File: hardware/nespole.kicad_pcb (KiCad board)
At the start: 2 copper layers, 87.9 x 54.9 mm, 45 parts, among them IC1 ATMEGA328PB-A, J1 Screw_Terminal_1x02, J2 Screw_Terminal_1x02, J3 Screw_Terminal_1x05, J4 Screw_Terminal_1x02, P1 USB_OTG, Q1 MJE13009G, Q2 MOSFET_P_CH, SW1 Rotary_Encoder_Switch, U1 MAX6675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

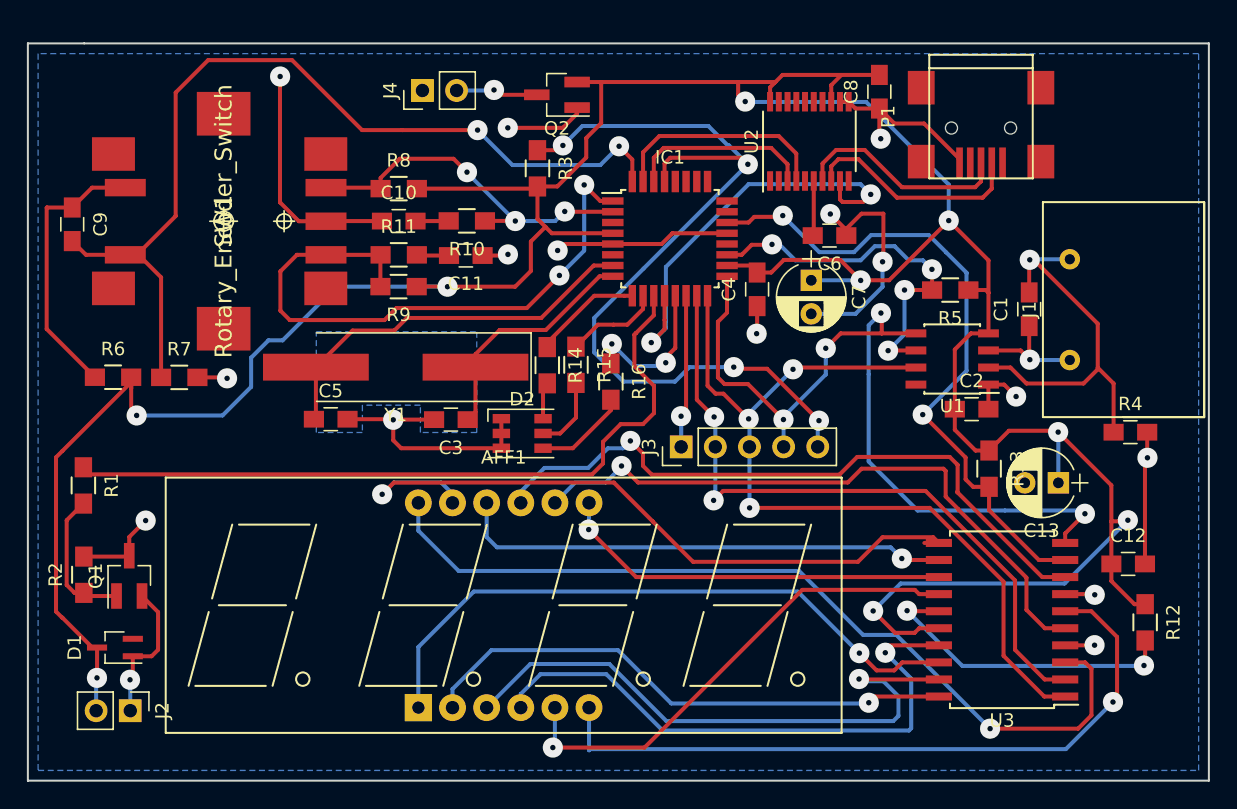
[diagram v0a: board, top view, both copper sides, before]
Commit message: Minor layout changes; exposing I2C bus via header.
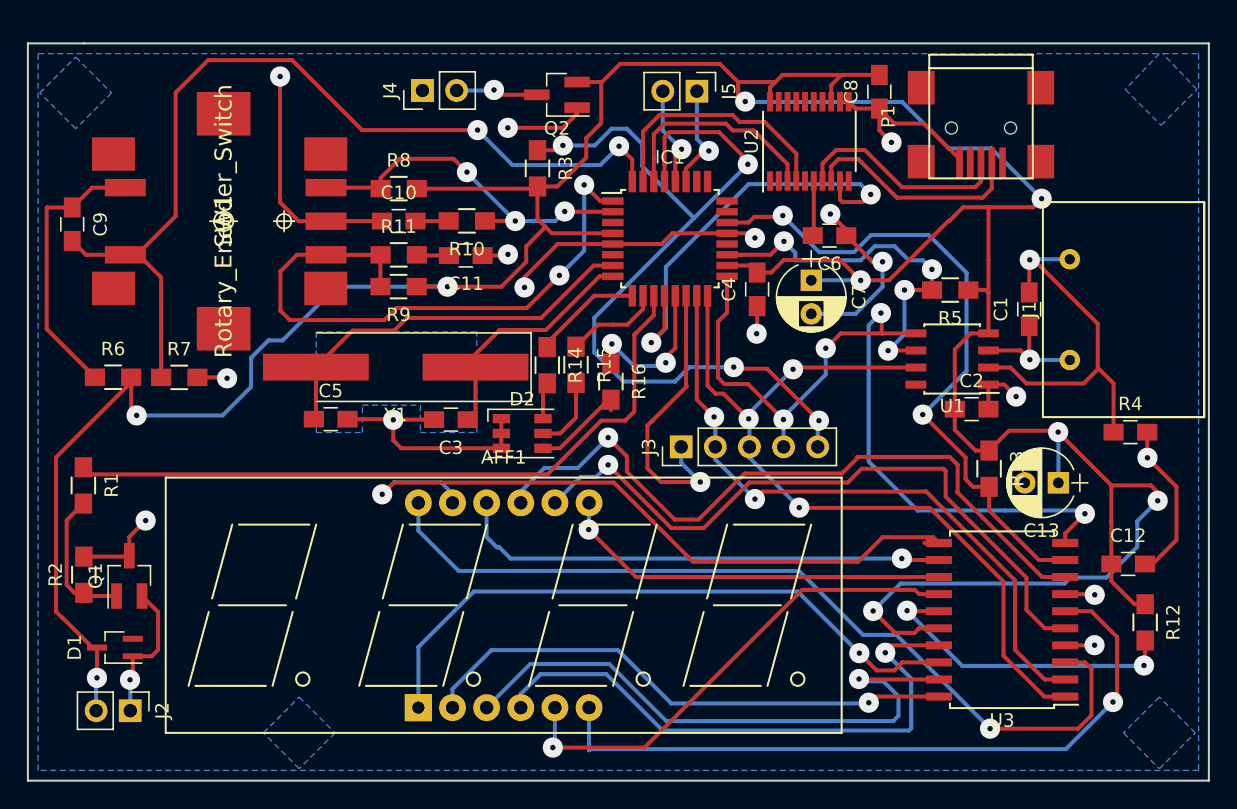
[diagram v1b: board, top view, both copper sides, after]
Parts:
- added J5: Screw_Terminal_1x02, Pin_Headers:Pin_Header_Straight_1x02_Pitch2.54mm, F.Cu at (154.4, 104.4)
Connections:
- IC1 pad 27: Net-(IC1-Pad27) -> SDA
- IC1 pad 28: Net-(IC1-Pad28) -> SCL
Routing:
- net +5V: track 252.2 -> 271.8 mm
- net MC_CS: track 11.4 -> 22.6 mm
- net SDA: track 0.00 -> 8.02 mm, vias 0 -> 1
- net SCL: track 0.00 -> 7.64 mm, vias 0 -> 1
- net GND: track 117.2 -> 123.2 mm, vias 15 -> 16
- net Net-(AFF1-Pad9): track 50.0 -> 53.2 mm
- net ENABLE_RELAY: track 55.5 -> 52.4 mm
- net Net-(AFF1-Pad8): track 47.6 -> 50.5 mm
- net RXD: track 13.8 -> 16.3 mm
- net TXD: track 16.7 -> 18.9 mm
- net MISO: track 64.2 -> 62.0 mm
- net RESET: track 65.9 -> 68.0 mm
- net MOSI: track 51.1 -> 49.1 mm
- net TEMP_CS: track 27.9 -> 29.5 mm

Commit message: Whoops; neglected to press the PCB update button.
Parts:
- R14, R15, R16: value 10k -> ?
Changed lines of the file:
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@@
     (links 119)
     (no_connects 0)
-    (area 104.572999 96.065819 194.8245 158.772381)
+    (area 104.572999 100.762999 192.607001 155.777001)
     (thickness 1.6)
     (drawings 9)
@@
       (effects (font (size 1 1) (thickness 0.15)))
     )
-    (fp_text value 10k (at 0 2.1 270) (layer F.Fab)
+    (fp_text value ? (at 0 2.1 270) (layer F.Fab)
       (effects (font (size 1 1) (thickness 0.15)))
     )
@@
       (effects (font (size 1 1) (thickness 0.15)))
     )
-    (fp_text value 10k (at 0 2.1 270) (layer F.Fab)
+    (fp_text value ? (at 0 2.1 270) (layer F.Fab)
       (effects (font (size 1 1) (thickness 0.15)))
     )
@@
       (effects (font (size 1 1) (thickness 0.15)))
     )
-    (fp_text value 10k (at 0 2.1 270) (layer F.Fab)
+    (fp_text value ? (at 0 2.1 270) (layer F.Fab)
       (effects (font (size 1 1) (thickness 0.15)))
     )
@@
   (segment (start 141.605 118.237) (end 141.605 118.999) (width 0.3) (layer F.Cu) (net 2))
   (segment (start 144.0752 115.7668) (end 141.605 118.237) (width 0.3) (layer F.Cu) (net 2))
-  (segment (start 156.6754 114.9668) (end 158.4008 114.9668) (width 0.3) (layer F.Cu) (net 2) (status 400000))
+  (segment (start 156.6754 114.9668) (end 158.4008 114.9668) (width 0.3) (layer F.Cu) (net 2))
   (via (at 158.75 115.316) (size 1.5) (drill 0.4) (layers F.Cu B.Cu) (net 2))
   (segment (start 158.4008 114.9668) (end 158.75 115.316) (width 0.3) (layer F.Cu) (net 2))
-  (segment (start 187.7749 139.573) (end 188.341 139.573) (width 0.3) (layer F.Cu) (net 2) (status C00000))
-  (segment (start 188.341 139.573) (end 190.119 137.795) (width 0.3) (layer F.Cu) (net 2) (status 400000))
+  (segment (start 187.7749 139.573) (end 188.341 139.573) (width 0.3) (layer F.Cu) (net 2))
+  (segment (start 188.341 139.573) (end 190.119 137.795) (width 0.3) (layer F.Cu) (net 2))
   (via (at 187.96 131.6736) (size 1.5) (drill 0.4) (layers F.Cu B.Cu) (net 2))
   (segment (start 190.119 133.8326) (end 187.96 131.6736) (width 0.3) (layer F.Cu) (net 2))
@@
   (segment (start 111.8997 111.57204) (end 112.98428 111.57204) (width 0.3) (layer F.Cu) (net 19))
   (segment (start 111.8997 111.57204) (end 111.8997 111.90478) (width 0.3) (layer F.Cu) (net 19))
-  (segment (start 156.6754 116.5668) (end 159.9122 116.5668) (width 0.3) (layer F.Cu) (net 20) (status 400000))
+  (segment (start 156.6754 116.5668) (end 159.9122 116.5668) (width 0.3) (layer F.Cu) (net 20))
   (segment (start 170.20032 116.98224) (end 169.14876 115.93068) (width 0.3) (layer B.Cu) (net 20))
   (segment (start 169.14876 115.93068) (end 167.67048 115.93068) (width 0.3) (layer B.Cu) (net 20))
@@
   (segment (start 155.99664 121.55424) (end 155.99664 125.69952) (width 0.3) (layer F.Cu) (net 23))
   (segment (start 156.6754 120.87548) (end 155.99664 121.55424) (width 0.3) (layer F.Cu) (net 23))
-  (segment (start 158.3436 130.8608) (end 158.3436 131.6736) (width 0.3) (layer B.Cu) (net 24) (status C00000))
-  (segment (start 158.3436 131.6736) (end 162.052 135.382) (width 0.3) (layer B.Cu) (net 24) (status 400000))
+  (segment (start 158.3436 130.8608) (end 158.3436 131.6736) (width 0.3) (layer B.Cu) (net 24))
+  (segment (start 158.3436 131.6736) (end 162.052 135.382) (width 0.3) (layer B.Cu) (net 24))
   (segment (start 180.28666 149.4409) (end 177.25136 146.4056) (width 0.3) (layer F.Cu) (net 24))
   (segment (start 177.25136 146.4056) (end 177.25136 140.8938) (width 0.3) (layer F.Cu) (net 24))
@@
   (segment (start 155.81884 126.90348) (end 156.40812 126.90348) (width 0.3) (layer F.Cu) (net 24))
   (segment (start 155.2254 126.31004) (end 155.81884 126.90348) (width 0.3) (layer F.Cu) (net 24))
-  (segment (start 155.8036 130.8608) (end 155.8036 131.8006) (width 0.3) (layer B.Cu) (net 25) (status 400000))
+  (segment (start 155.8036 130.8608) (end 155.8036 131.8006) (width 0.3) (layer B.Cu) (net 25))
   (segment (start 159.30626 134.19074) (end 171.49826 134.19074) (width 0.3) (layer F.Cu) (net 25))
   (segment (start 158.75 134.747) (end 159.30626 134.19074) (width 0.3) (layer F.Cu) (net 25))
@@
   (via (at 155.71216 128.63576) (size 1.5) (drill 0.4) (layers F.Cu B.Cu) (net 25))
   (segment (start 154.4254 127.349) (end 155.71216 128.63576) (width 0.3) (layer F.Cu) (net 25))
-  (segment (start 153.2636 130.8608) (end 153.2636 132.0546) (width 0.3) (layer B.Cu) (net 26) (status 400000))
+  (segment (start 153.2636 130.8608) (end 153.2636 132.0546) (width 0.3) (layer B.Cu) (net 26))
   (segment (start 150.749 129.286) (end 151.13 128.905) (width 0.3) (layer F.Cu) (net 26))
   (segment (start 150.749 132.461) (end 150.749 129.286) (width 0.3) (layer F.Cu) (net 26))
@@
   (via (at 154.686 133.477) (size 1.5) (drill 0.4) (layers F.Cu B.Cu) (net 26))
   (segment (start 153.2636 132.0546) (end 154.686 133.477) (width 0.3) (layer B.Cu) (net 26))
-  (segment (start 153.2636 130.8608) (end 153.2636 131.5974) (width 0.3) (layer B.Cu) (net 26) (status C00000))
+  (segment (start 153.2636 130.8608) (end 153.2636 131.5974) (width 0.3) (layer B.Cu) (net 26))
   (segment (start 151.003 129.032) (end 151.13 128.905) (width 0.3) (layer F.Cu) (net 26))
   (segment (start 151.13 128.905) (end 153.6254 126.4096) (width 0.3) (layer F.Cu) (net 26))
@@
   (segment (start 142.8496 121.26976) (end 132.85216 121.26976) (width 0.3) (layer F.Cu) (net 60))
   (segment (start 146.75256 117.3668) (end 142.8496 121.26976) (width 0.3) (layer F.Cu) (net 60))
-  (segment (start 142.98228 130.96512) (end 144.24388 130.96512) (width 0.3) (layer F.Cu) (net 63) (status 400000))
-  (segment (start 144.24388 130.96512) (end 147.85468 127.35432) (width 0.3) (layer F.Cu) (net 63) (status 800000))
-  (segment (start 147.85468 127.35432) (end 148.0312 127.35432) (width 0.3) (layer F.Cu) (net 63) (status C00000))
+  (segment (start 142.98228 130.96512) (end 144.24388 130.96512) (width 0.3) (layer F.Cu) (net 63))
+  (segment (start 144.24388 130.96512) (end 147.85468 127.35432) (width 0.3) (layer F.Cu) (net 63))
+  (segment (start 147.85468 127.35432) (end 148.0312 127.35432) (width 0.3) (layer F.Cu) (net 63))
   (segment (start 148.0312 128.13284) (end 148.0312 127.35432) (width 0.3) (layer F.Cu) (net 63))
   (segment (start 148.0312 124.65432) (end 148.0312 123.27128) (width 0.3) (layer F.Cu) (net 64))

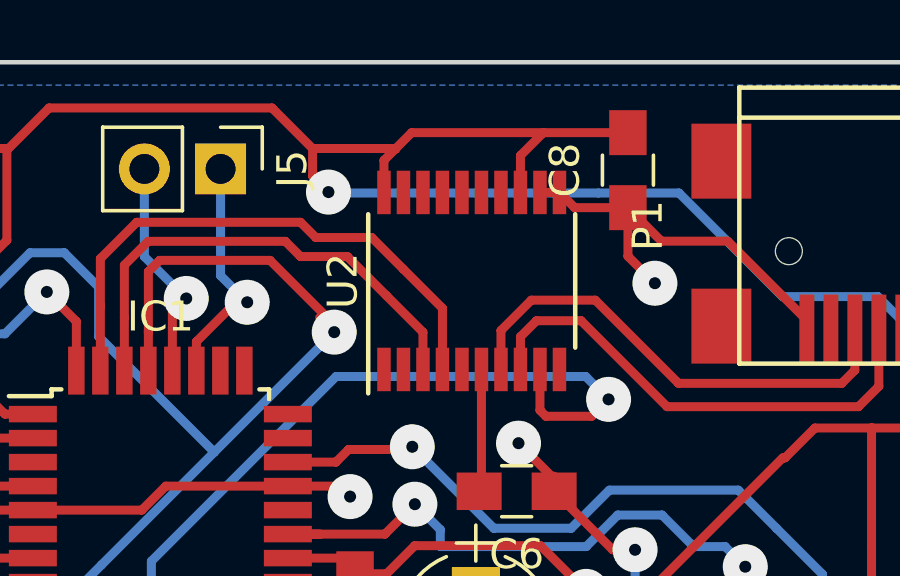
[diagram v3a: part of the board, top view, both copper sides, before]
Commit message: I'm glad I checked -- the CH341T has a slightly wider size from normal TSSOP-20s.
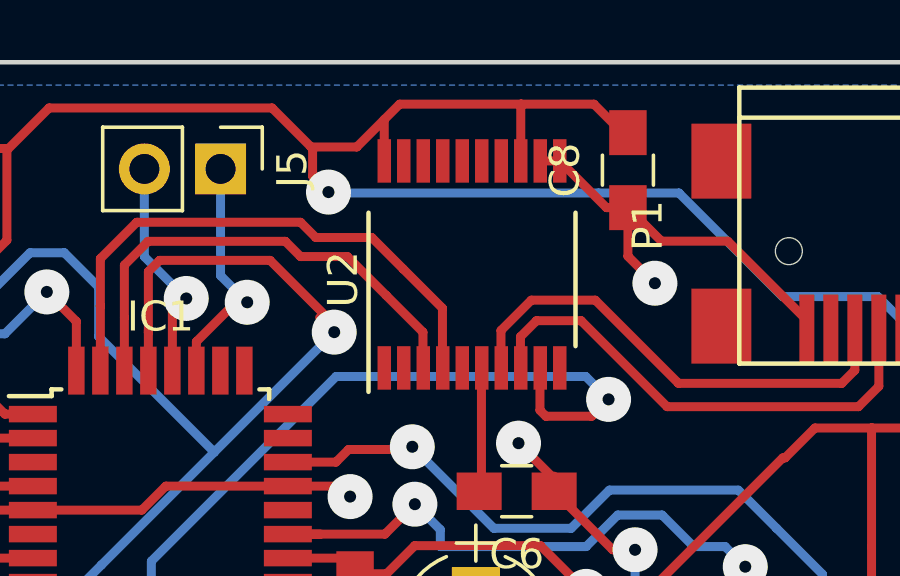
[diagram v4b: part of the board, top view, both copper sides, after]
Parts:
- U2: footprint Housings_SSOP:TSSOP-20_4.4x6.5mm_Pitch0.65mm -> nespole:TSSOP-20_CH341T
- moved U2 0.05 mm to (162.8, 108.1)

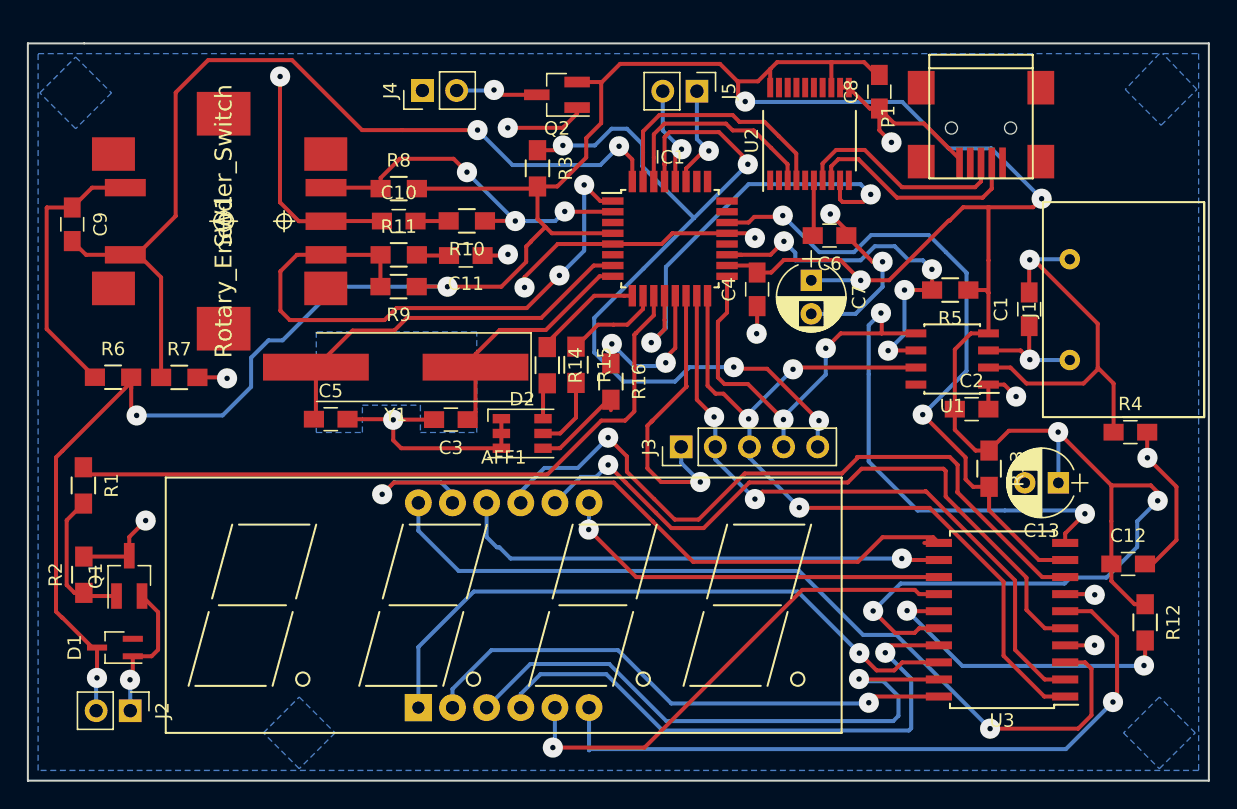
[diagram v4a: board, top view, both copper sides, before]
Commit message: Increase traces to 0.5mm; swap CH341T with CH340G; add USB power jumper.
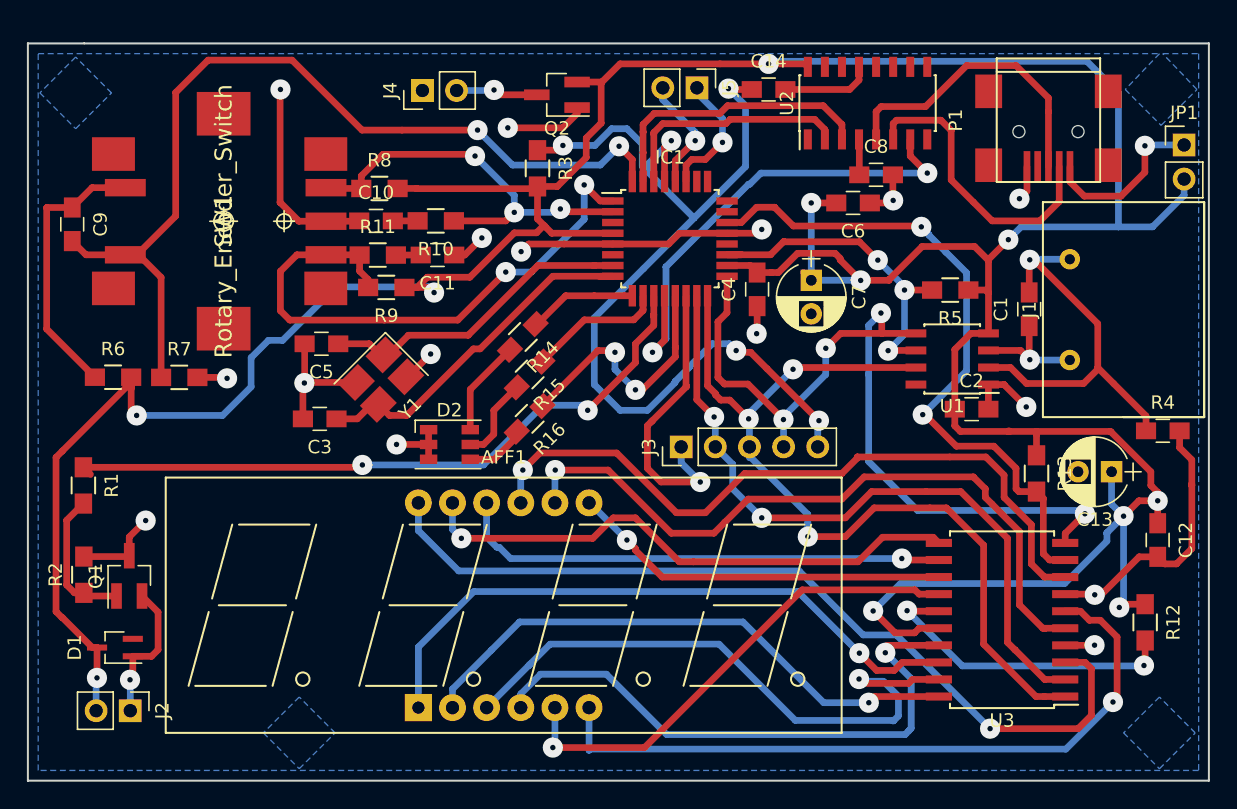
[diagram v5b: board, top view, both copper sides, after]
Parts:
- added C14: 0.1u, Capacitors_SMD:C_0805_HandSoldering, F.Cu at (159.8, 104.3)
- added JP1: Jumper_NO_Small, Pin_Headers:Pin_Header_Straight_1x02_Pitch2.54mm, F.Cu at (190.7, 108.4)
- U2: value CH341T -> CH340G; footprint nespole:TSSOP-20_CH341T -> Housings_SOIC:SOIC-16_3.9x9.9mm_Pitch1.27mm
- Y1: value 12M -> Crystal_GND24; footprint Crystals:Crystal_SMD_HC49-SD_HandSoldering -> Crystals:Crystal_SMD_TXC_7M-4pin_3.2x2.5mm_HandSoldering
- moved C3 9.76 mm to (126.4, 128.8)
- moved R16 6.65 mm to (142.0, 128.8), turned to 225 degrees
- moved C8 6.19 mm to (167.8, 110.6), turned to 0 degrees
- moved C5 5.66 mm to (126.5, 123.2), turned to 180 degrees
- moved D2 5.48 mm to (136.0, 130.7)
- moved U2 5.14 mm to (167.1, 105.3)
- moved P1 5.03 mm to (180.6, 106.6)
- moved C13 4.05 mm to (185.3, 132.7)
- moved R13 3.55 mm to (179.7, 132.8)
- moved R15 3.52 mm to (142.0, 125.5), turned to 225 degrees
- moved C6 2.99 mm to (166.1, 112.7)
- moved C12 2.83 mm to (188.7, 137.8), turned to 270 degrees
- moved R14 2.78 mm to (141.5, 122.7), turned to 225 degrees
- moved R4 2.42 mm to (189.1, 129.7)
- moved R10 2.31 mm to (135.0, 114.0)
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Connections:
- C6 pad 2: Net-(C6-Pad2) -> +5V
- C8 pad 1: GND -> Net-(C8-Pad1)
- C8 pad 2: +5V -> GND
- U2 pad 11: GND -> Net-(U2-Pad11)
- U2 pad 12: GND -> Net-(U2-Pad12)
- U2 pad 13: +5V -> Net-(C14-Pad2)
- U2 pad 16: Net-(U2-Pad16) -> +5V
- U2 pad 2: Net-(U2-Pad2) -> RXD
- U2 pad 3: RXD -> TXD
- U2 pad 4: TXD -> Net-(C8-Pad1)
- U2 pad 5: Net-(U2-Pad5) -> Net-(P1-Pad3)
- U2 pad 6: Net-(C6-Pad2) -> Net-(P1-Pad2)
- U2 pad 7: Net-(P1-Pad3) -> CLKOUT
- U2 pad 8: Net-(P1-Pad2) -> Net-(U2-Pad8)
- U2 pad 9: CLKOUT -> Net-(U2-Pad9)
- Y1 pad 1: Net-(C3-Pad1) -> Net-(C5-Pad1)
- Y1 pad 2: Net-(C5-Pad1) -> GND
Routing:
- net +5V: track 271.9 -> 293.6 mm, vias 9 -> 11
- net GND: track 123.6 -> 104.1 mm
- net Net-(JP1-Pad1): track 0.00 -> 12.8 mm, vias 0 -> 1
- net Net-(AFF1-Pad11): track 52.9 -> 42.1 mm
- net Net-(C3-Pad1): track 18.8 -> 26.6 mm
- net LED_B: track 11.6 -> 19.3 mm
- net RESET: track 68.0 -> 75.3 mm, vias 4 -> 5
- net Net-(C14-Pad2): track 0.00 -> 6.76 mm
- net Net-(P1-Pad3): track 16.2 -> 22.4 mm
- net Net-(C5-Pad1): track 29.2 -> 23.6 mm
- net Net-(P1-Pad2): track 16.6 -> 22.2 mm
- net CLKOUT: track 32.1 -> 36.7 mm
- net MISO: track 62.0 -> 66.6 mm
- net Net-(D2-Pad6): track 2.76 -> 7.17 mm
- net Net-(C6-Pad2): track 4.09 -> 0.00 mm
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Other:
- net class Default: trace_width 0.3 -> 0.5

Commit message: Better ground plane unity.
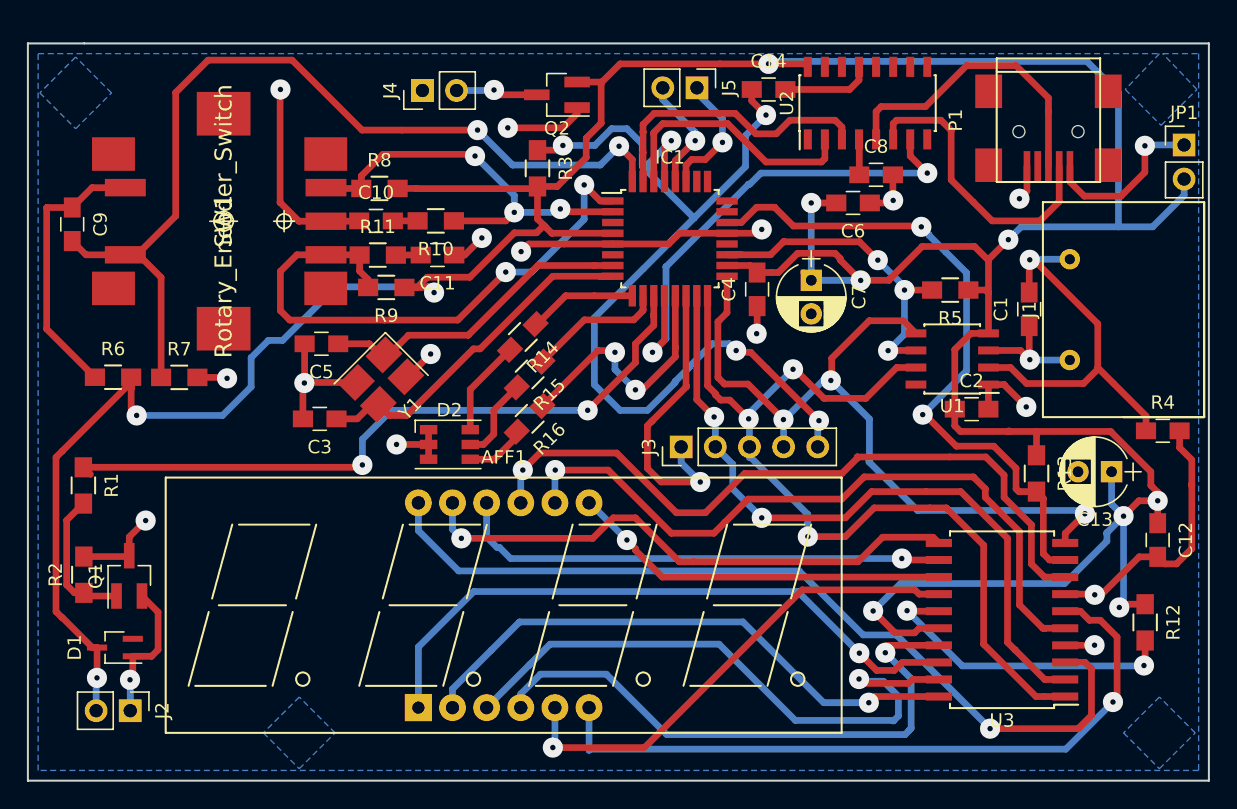
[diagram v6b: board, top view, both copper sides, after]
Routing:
- net SCK: track 63.2 -> 58.2 mm, vias 4 -> 3
- net MISO: track 66.6 -> 68.6 mm
- net RXD: track 17.8 -> 19.4 mm
- net ENABLE_RELAY: track 50.9 -> 52.3 mm
- net RESET: track 75.3 -> 74.1 mm
